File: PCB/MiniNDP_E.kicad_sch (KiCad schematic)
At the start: 20 parts, among them J1 Conn_02x20_Odd_Even, U1 HC161, U2 HC161, U3 HC161, U4 HC138, U5 HC574, U6 AS6C4008, U7 1G32, U8 1G79

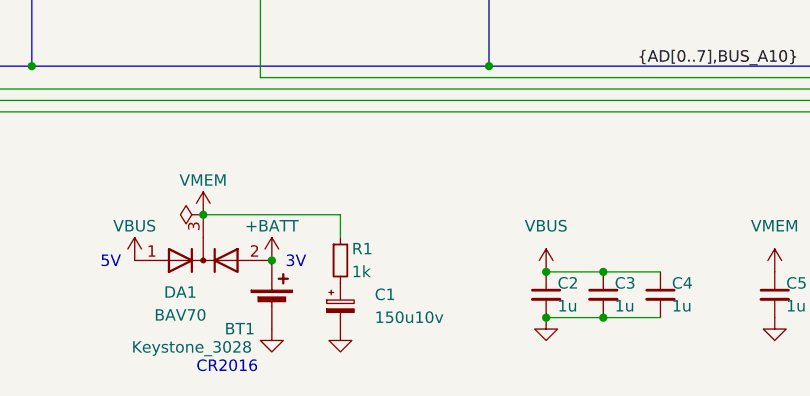
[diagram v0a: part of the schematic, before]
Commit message: rename 512_F to EZ512
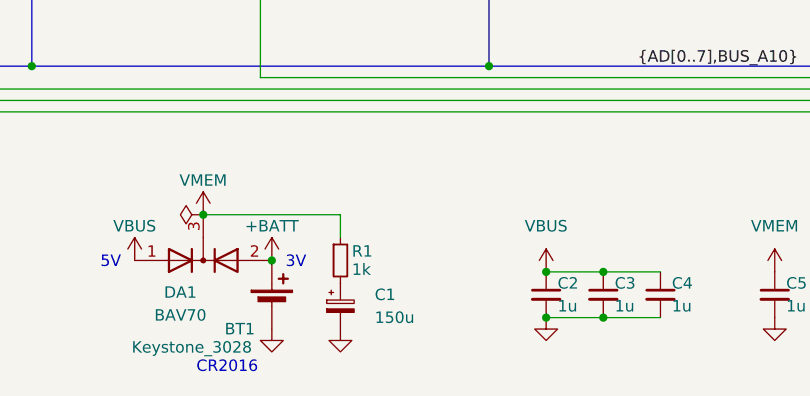
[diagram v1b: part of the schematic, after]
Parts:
- C1: value 150u10v -> 150u
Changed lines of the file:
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@@
 			)
 		)
-		(property "Value" "150u10v"
+		(property "Value" "150u"
 			(at 114.3 186.69 0)
 			(effects
@@
 		(dnp no)
 		(property "Reference" "R1"
-			(at 111.76 179.07 0)
+			(at 111.76 179.324 0)
 			(effects
 				(font
@@
 		)
 		(property "Value" "1k"
-			(at 111.76 181.61 0)
+			(at 111.76 181.356 0)
 			(effects
 				(font
